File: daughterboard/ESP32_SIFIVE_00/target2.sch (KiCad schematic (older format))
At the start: 0 parts

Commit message: further work on ESP32/SIFIVE daughterboard
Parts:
- added C?: 10u, symbol Device:C_Small
- added R? (x2): 10k, symbol Device:R_Small
- added U?: LoFive-R1, hive_daughterboard:LoFive-R1, symbol hive_daughterboard:LoFive-R1
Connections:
- net +3V3: now also R?.2
- net +5V: now also C?.1, U?.1 (+5V)
- net GPIO2.0: now also U?.24 (GPIO_20/PWM1.0)
- net GPIO2.1: now also U?.25 (GPIO_21/PWM1.2)
- net GPIO2.2: now also U?.26 (GPIO_22/PWM1.3)
- net GPIO2.3: now also U?.27 (GPIO_23)
- net RST_2: now also U?.4 (JTAG_TRST_N)
- net TCK|SWDCLK_2: now also R?.1, U?.5 (JTAG_TCK)
- net TDI|NC_2: now also U?.8 (JTAG_TDI)
- net TDO|SWO_2: now also U?.6 (JTAG_TDO)
- net TMS|SWDIO_2: now also R?.1, U?.7 (JTAG_TMS)
- net UART_RxD2: now also U?.21 (GPIO_17/UART0.TX)
- net UART_TxD2: now also U?.20 (GPIO_16/UART0.RX)
- new net GND: C?.2, R?.2, U?.2 (GND), U?.28 (GND)
- no-connect marks 0 -> 14
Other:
- note removed: "Power"

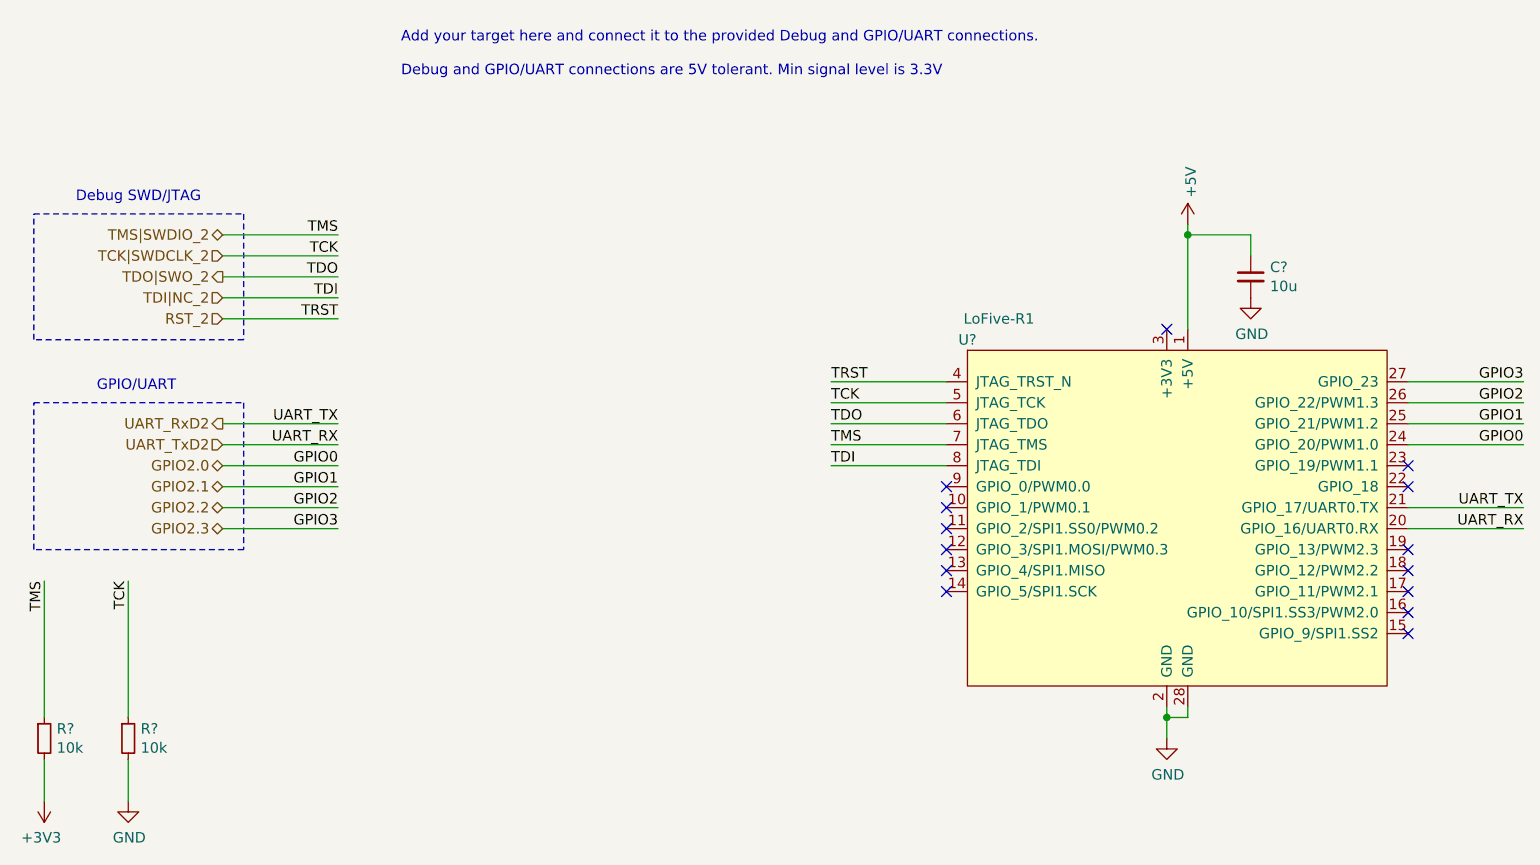
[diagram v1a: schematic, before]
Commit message: ERC on daughterboards
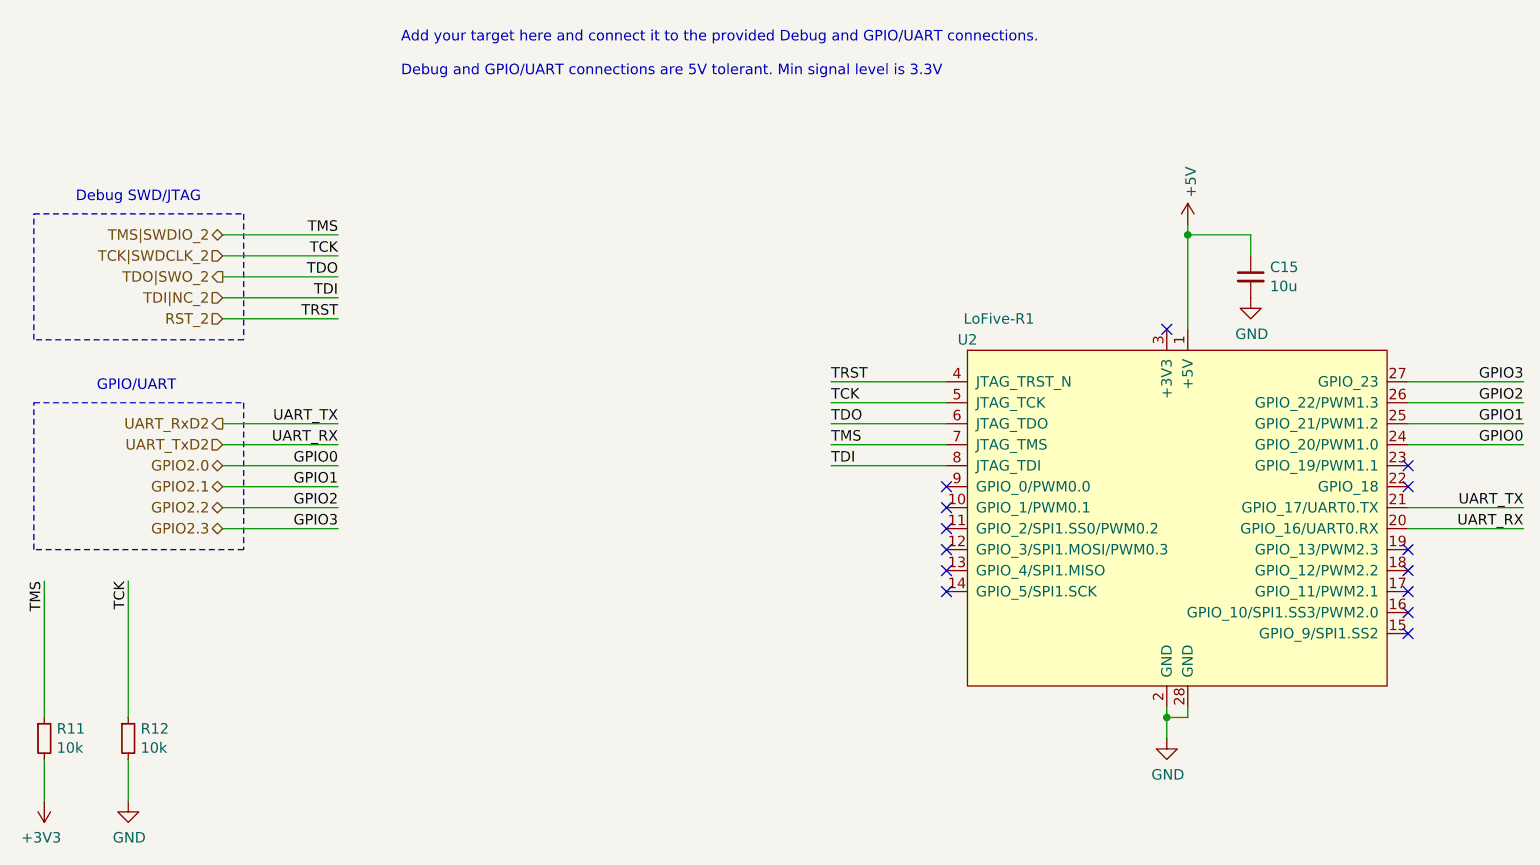
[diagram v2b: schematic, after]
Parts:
- gave numbers to parts that had none: 4
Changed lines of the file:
@@
 Add your target here and connect it to the provided Debug and GPIO/UART connections.\n\nDebug and GPIO/UART connections are 5V tolerant. Min signal level is 3.3V
 $Comp
-L hive_daughterboard:LoFive-R1 U?
+L hive_daughterboard:LoFive-R1 U2
 U 1 1 618DA905
 P 6200 2250
-F 0 "U?" H 5200 2300 50  0000 C CNN
+F 0 "U2" H 5200 2300 50  0000 C CNN
 F 1 "LoFive-R1" H 5350 2400 50  0000 C CNN
 F 2 "hive_daughterboard:LoFive-R1" H 6200 2250 50  0001 C CNN
@@
 P 6250 1650
 AR Path="/61668514/618DDE96" Ref="#PWR?"  Part="1"
-AR Path="/616688D6/618DDE96" Ref="#PWR?"  Part="1"
-F 0 "#PWR?" H 6250 1500 50  0001 C CNN
+AR Path="/616688D6/618DDE96" Ref="#PWR0136"  Part="1"
+F 0 "#PWR0136" H 6250 1500 50  0001 C CNN
 F 1 "+5V" V 6265 1778 50  0000 L CNN
 F 2 "" H 6250 1650 50  0001 C CNN
@@
 $EndComp
 $Comp
-L Device:C_Small C?
+L Device:C_Small C15
 U 1 1 618DFA96
 P 6550 1900
-F 0 "C?" H 6642 1946 50  0000 L CNN
+F 0 "C15" H 6642 1946 50  0000 L CNN
 F 1 "10u" H 6642 1855 50  0000 L CNN
 F 2 "" H 6550 1900 50  0001 C CNN
@@
 NoConn ~ 6150 2150
 $Comp
-L power:GND #PWR?
+L power:GND #PWR0137
 U 1 1 618E074B
 P 6550 2000
-F 0 "#PWR?" H 6550 1750 50  0001 C CNN
+F 0 "#PWR0137" H 6550 1750 50  0001 C CNN
 F 1 "GND" H 6555 1827 50  0000 C CNN
 F 2 "" H 6550 2000 50  0001 C CNN
@@
 	6250 1700 6250 1650
 $Comp
-L power:GND #PWR?
+L power:GND #PWR0138
 U 1 1 618E218D
 P 6150 4100
-F 0 "#PWR?" H 6150 3850 50  0001 C CNN
+F 0 "#PWR0138" H 6150 3850 50  0001 C CNN
 F 1 "GND" H 6155 3927 50  0000 C CNN
 F 2 "" H 6150 4100 50  0001 C CNN
@@
 TMS
 $Comp
-L Device:R_Small R?
+L Device:R_Small R12
 U 1 1 618ED1FE
 P 1200 4100
-F 0 "R?" H 1259 4146 50  0000 L CNN
+F 0 "R12" H 1259 4146 50  0000 L CNN
 F 1 "10k" H 1259 4055 50  0000 L CNN
 F 2 "" H 1200 4100 50  0001 C CNN
@@
 $EndComp
 $Comp
-L power:GND #PWR?
+L power:GND #PWR0139
 U 1 1 618EDFCC
 P 1200 4400
-F 0 "#PWR?" H 1200 4150 50  0001 C CNN
+F 0 "#PWR0139" H 1200 4150 50  0001 C CNN
 F 1 "GND" H 1205 4227 50  0000 C CNN
 F 2 "" H 1200 4400 50  0001 C CNN
@@
 	1200 4400 1200 4200
 $Comp
-L Device:R_Small R?
+L Device:R_Small R11
 U 1 1 618F4230
 P 800 4100
-F 0 "R?" H 859 4146 50  0000 L CNN
+F 0 "R11" H 859 4146 50  0000 L CNN
 F 1 "10k" H 859 4055 50  0000 L CNN
 F 2 "" H 800 4100 50  0001 C CNN
@@
 	800  3350 800  4000
 $Comp
-L power:+3V3 #PWR?
+L power:+3V3 #PWR0140
 U 1 1 618F94CF
 P 800 4400
-F 0 "#PWR?" H 800 4250 50  0001 C CNN
+F 0 "#PWR0140" H 800 4250 50  0001 C CNN
 F 1 "+3V3" H 815 4573 50  0000 C CNN
 F 2 "" H 800 4400 50  0001 C CNN

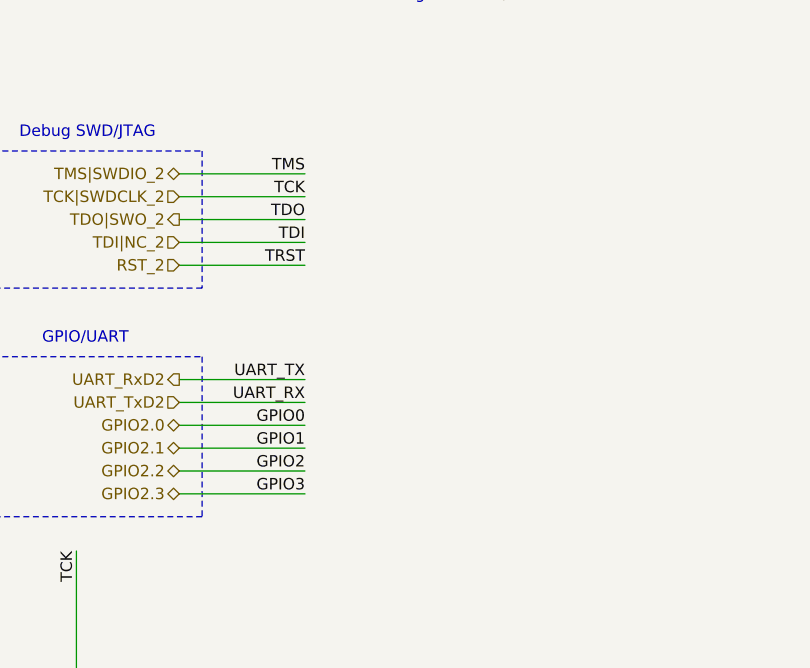
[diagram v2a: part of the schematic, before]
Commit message: added testpoints to daughterboards, updated readme
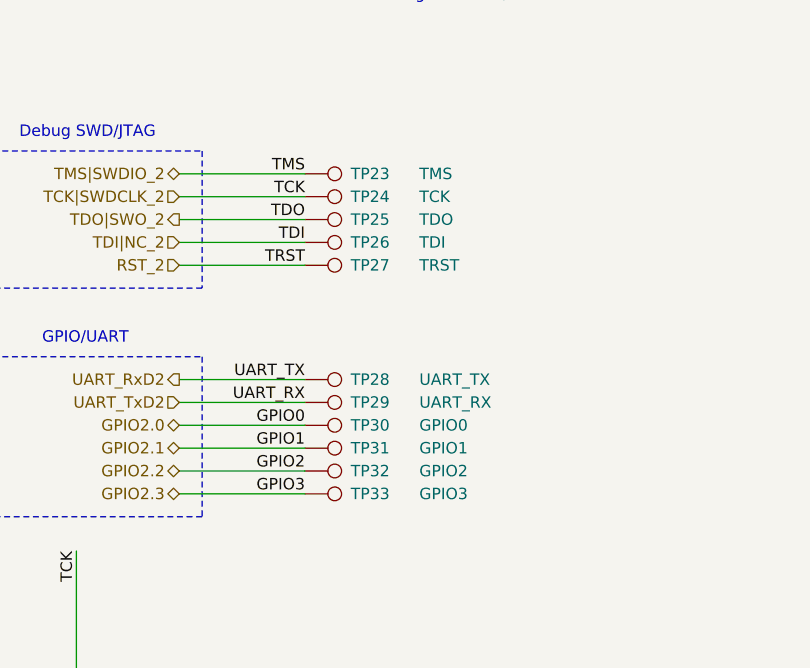
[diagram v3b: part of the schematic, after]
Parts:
- added TP23: TMS, symbol Connector:TestPoint
- added TP24: TCK, symbol Connector:TestPoint
- added TP25: TDO, symbol Connector:TestPoint
- added TP26: TDI, symbol Connector:TestPoint
- added TP27: TRST, symbol Connector:TestPoint
- added TP28: UART_TX, symbol Connector:TestPoint
- added TP29: UART_RX, symbol Connector:TestPoint
- added TP30: GPIO0, symbol Connector:TestPoint
- added TP31: GPIO1, symbol Connector:TestPoint
- added TP32: GPIO2, symbol Connector:TestPoint
- added TP33: GPIO3, symbol Connector:TestPoint
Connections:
- net GPIO2.0: now also TP30.1
- net GPIO2.1: now also TP31.1
- net GPIO2.2: now also TP32.1
- net GPIO2.3: now also TP33.1
- net RST_2: now also TP27.1
- net TCK|SWDCLK_2: now also TP24.1
- net TDI|NC_2: now also TP26.1
- net TDO|SWO_2: now also TP25.1
- net TMS|SWDIO_2: now also TP23.1
- net UART_RxD2: now also TP28.1
- net UART_TxD2: now also TP29.1
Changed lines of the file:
@@
 	-1   0    0    1
 $EndComp
+$Comp
+L Connector:TestPoint TP23
+U 1 1 61906846
+P 2200 1700
+F 0 "TP23" V 2200 1900 50  0000 L CNN
+F 1 "TMS" V 2200 2200 50  0000 L CNN
+F 2 "" H 2400 1700 50  0001 C CNN
+F 3 "~" H 2400 1700 50  0001 C CNN
+	1    2200 1700
+	0    1    1    0
+$EndComp
+$Comp
+L Connector:TestPoint TP24
+U 1 1 6190873D
+P 2200 1800
+F 0 "TP24" V 2200 2000 50  0000 L CNN
+F 1 "TCK" V 2200 2300 50  0000 L CNN
+F 2 "" H 2400 1800 50  0001 C CNN
+F 3 "~" H 2400 1800 50  0001 C CNN
+	1    2200 1800
+	0    1    1    0
+$EndComp
+$Comp
+L Connector:TestPoint TP25
+U 1 1 619088C7
+P 2200 1900
+F 0 "TP25" V 2200 2100 50  0000 L CNN
+F 1 "TDO" V 2200 2400 50  0000 L CNN
+F 2 "" H 2400 1900 50  0001 C CNN
+F 3 "~" H 2400 1900 50  0001 C CNN
+	1    2200 1900
+	0    1    1    0
+$EndComp
+$Comp
+L Connector:TestPoint TP26
+U 1 1 61908AEF
+P 2200 2000
+F 0 "TP26" V 2200 2200 50  0000 L CNN
+F 1 "TDI" V 2200 2500 50  0000 L CNN
+F 2 "" H 2400 2000 50  0001 C CNN
+F 3 "~" H 2400 2000 50  0001 C CNN
+	1    2200 2000
+	0    1    1    0
+$EndComp
+$Comp
+L Connector:TestPoint TP27
+U 1 1 61908CE1
+P 2200 2100
+F 0 "TP27" V 2200 2300 50  0000 L CNN
+F 1 "TRST" V 2200 2600 50  0000 L CNN
+F 2 "" H 2400 2100 50  0001 C CNN
+F 3 "~" H 2400 2100 50  0001 C CNN
+	1    2200 2100
+	0    1    1    0
+$EndComp
+$Comp
+L Connector:TestPoint TP28
+U 1 1 61908F07
+P 2200 2600
+F 0 "TP28" V 2200 2800 50  0000 L CNN
+F 1 "UART_TX" V 2200 3100 50  0000 L CNN
+F 2 "" H 2400 2600 50  0001 C CNN
+F 3 "~" H 2400 2600 50  0001 C CNN
+	1    2200 2600
+	0    1    1    0
+$EndComp
+$Comp
+L Connector:TestPoint TP29
+U 1 1 61909318
+P 2200 2700
+F 0 "TP29" V 2200 2900 50  0000 L CNN
+F 1 "UART_RX" V 2200 3200 50  0000 L CNN
+F 2 "" H 2400 2700 50  0001 C CNN
+F 3 "~" H 2400 2700 50  0001 C CNN
+	1    2200 2700
+	0    1    1    0
+$EndComp
+$Comp
+L Connector:TestPoint TP30
+U 1 1 6190965A
+P 2200 2800
+F 0 "TP30" V 2200 3000 50  0000 L CNN
+F 1 "GPIO0" V 2200 3300 50  0000 L CNN
+F 2 "" H 2400 2800 50  0001 C CNN
+F 3 "~" H 2400 2800 50  0001 C CNN
+	1    2200 2800
+	0    1    1    0
+$EndComp
+$Comp
+L Connector:TestPoint TP31
+U 1 1 619098B5
+P 2200 2900
+F 0 "TP31" V 2200 3100 50  0000 L CNN
+F 1 "GPIO1" V 2200 3400 50  0000 L CNN
+F 2 "" H 2400 2900 50  0001 C CNN
+F 3 "~" H 2400 2900 50  0001 C CNN
+	1    2200 2900
+	0    1    1    0
+$EndComp
+$Comp
+L Connector:TestPoint TP32
+U 1 1 61909B12
+P 2200 3000
+F 0 "TP32" V 2200 3200 50  0000 L CNN
+F 1 "GPIO2" V 2200 3500 50  0000 L CNN
+F 2 "" H 2400 3000 50  0001 C CNN
+F 3 "~" H 2400 3000 50  0001 C CNN
+	1    2200 3000
+	0    1    1    0
+$EndComp
+$Comp
+L Connector:TestPoint TP33
+U 1 1 61909D32
+P 2200 3100
+F 0 "TP33" V 2200 3300 50  0000 L CNN
+F 1 "GPIO3" V 2200 3600 50  0000 L CNN
+F 2 "" H 2400 3100 50  0001 C CNN
+F 3 "~" H 2400 3100 50  0001 C CNN
+	1    2200 3100
+	0    1    1    0
+$EndComp
 $EndSCHEMATC

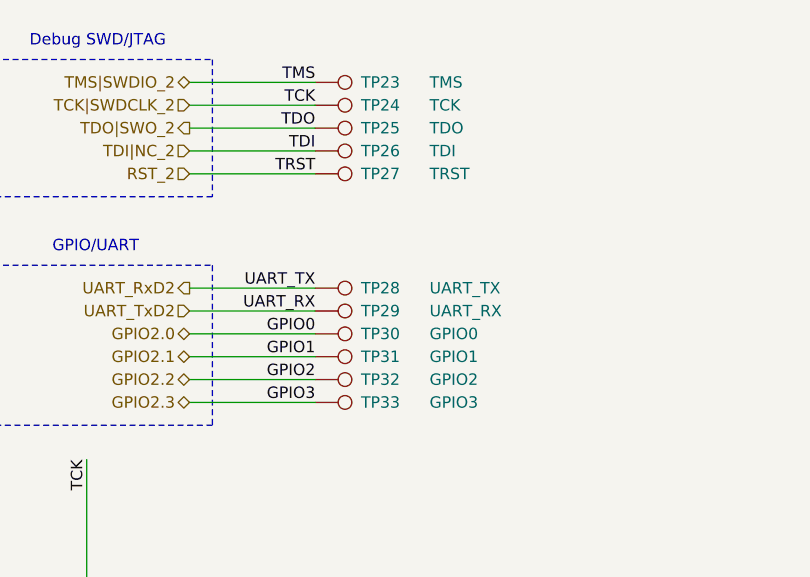
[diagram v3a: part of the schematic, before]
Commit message: started with esp32/sifive layout
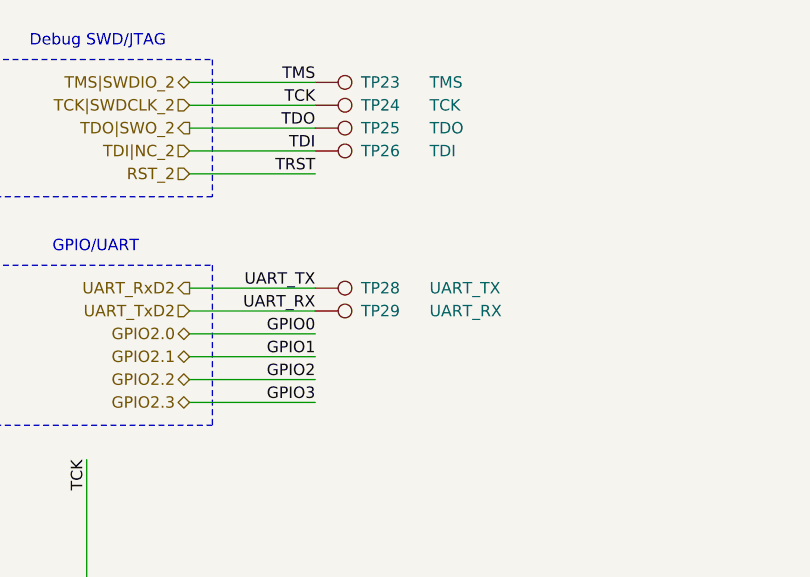
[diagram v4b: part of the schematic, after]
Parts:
- removed TP27: TRST, symbol Connector:TestPoint
- removed TP30: GPIO0, symbol Connector:TestPoint
- removed TP31: GPIO1, symbol Connector:TestPoint
- removed TP32: GPIO2, symbol Connector:TestPoint
- removed TP33: GPIO3, symbol Connector:TestPoint
- C15: footprint (none) -> Capacitor_SMD:C_0603_1608Metric_Pad1.05x0.95mm_HandSolder
- R11, R12: footprint (none) -> Resistor_SMD:R_0603_1608Metric_Pad1.05x0.95mm_HandSolder
- TP23, TP24, TP25, TP26, TP28, TP29: footprint (none) -> TestPoint:TestPoint_Pad_1.0x1.0mm
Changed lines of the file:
@@
 F 0 "C15" H 6642 1946 50  0000 L CNN
 F 1 "10u" H 6642 1855 50  0000 L CNN
-F 2 "" H 6550 1900 50  0001 C CNN
+F 2 "Capacitor_SMD:C_0603_1608Metric_Pad1.05x0.95mm_HandSolder" H 6550 1900 50  0001 C CNN
 F 3 "~" H 6550 1900 50  0001 C CNN
 	1    6550 1900
@@
 F 0 "R12" H 1259 4146 50  0000 L CNN
 F 1 "10k" H 1259 4055 50  0000 L CNN
-F 2 "" H 1200 4100 50  0001 C CNN
+F 2 "Resistor_SMD:R_0603_1608Metric_Pad1.05x0.95mm_HandSolder" H 1200 4100 50  0001 C CNN
 F 3 "~" H 1200 4100 50  0001 C CNN
 	1    1200 4100
@@
 F 0 "R11" H 859 4146 50  0000 L CNN
 F 1 "10k" H 859 4055 50  0000 L CNN
-F 2 "" H 800 4100 50  0001 C CNN
+F 2 "Resistor_SMD:R_0603_1608Metric_Pad1.05x0.95mm_HandSolder" H 800 4100 50  0001 C CNN
 F 3 "~" H 800 4100 50  0001 C CNN
 	1    800  4100
@@
 F 0 "TP23" V 2200 1900 50  0000 L CNN
 F 1 "TMS" V 2200 2200 50  0000 L CNN
-F 2 "" H 2400 1700 50  0001 C CNN
+F 2 "TestPoint:TestPoint_Pad_1.0x1.0mm" H 2400 1700 50  0001 C CNN
 F 3 "~" H 2400 1700 50  0001 C CNN
 	1    2200 1700
@@
 F 0 "TP24" V 2200 2000 50  0000 L CNN
 F 1 "TCK" V 2200 2300 50  0000 L CNN
-F 2 "" H 2400 1800 50  0001 C CNN
+F 2 "TestPoint:TestPoint_Pad_1.0x1.0mm" H 2400 1800 50  0001 C CNN
 F 3 "~" H 2400 1800 50  0001 C CNN
 	1    2200 1800
@@
 F 0 "TP25" V 2200 2100 50  0000 L CNN
 F 1 "TDO" V 2200 2400 50  0000 L CNN
-F 2 "" H 2400 1900 50  0001 C CNN
+F 2 "TestPoint:TestPoint_Pad_1.0x1.0mm" H 2400 1900 50  0001 C CNN
 F 3 "~" H 2400 1900 50  0001 C CNN
 	1    2200 1900
@@
 F 0 "TP26" V 2200 2200 50  0000 L CNN
 F 1 "TDI" V 2200 2500 50  0000 L CNN
-F 2 "" H 2400 2000 50  0001 C CNN
+F 2 "TestPoint:TestPoint_Pad_1.0x1.0mm" H 2400 2000 50  0001 C CNN
 F 3 "~" H 2400 2000 50  0001 C CNN
 	1    2200 2000
-	0    1    1    0
-$EndComp
-$Comp
-L Connector:TestPoint TP27
-U 1 1 61908CE1
-P 2200 2100
-F 0 "TP27" V 2200 2300 50  0000 L CNN
-F 1 "TRST" V 2200 2600 50  0000 L CNN
-F 2 "" H 2400 2100 50  0001 C CNN
-F 3 "~" H 2400 2100 50  0001 C CNN
-	1    2200 2100
 	0    1    1    0
 $EndComp
@@
 F 0 "TP28" V 2200 2800 50  0000 L CNN
 F 1 "UART_TX" V 2200 3100 50  0000 L CNN
-F 2 "" H 2400 2600 50  0001 C CNN
+F 2 "TestPoint:TestPoint_Pad_1.0x1.0mm" H 2400 2600 50  0001 C CNN
 F 3 "~" H 2400 2600 50  0001 C CNN
 	1    2200 2600
@@
 F 0 "TP29" V 2200 2900 50  0000 L CNN
 F 1 "UART_RX" V 2200 3200 50  0000 L CNN
-F 2 "" H 2400 2700 50  0001 C CNN
+F 2 "TestPoint:TestPoint_Pad_1.0x1.0mm" H 2400 2700 50  0001 C CNN
 F 3 "~" H 2400 2700 50  0001 C CNN
 	1    2200 2700
 	0    1    1    0
 $EndComp
-$Comp
-L Connector:TestPoint TP30
-U 1 1 6190965A
-P 2200 2800
-F 0 "TP30" V 2200 3000 50  0000 L CNN
-F 1 "GPIO0" V 2200 3300 50  0000 L CNN
-F 2 "" H 2400 2800 50  0001 C CNN
-F 3 "~" H 2400 2800 50  0001 C CNN
-	1    2200 2800
-	0    1    1    0
-$EndComp
-$Comp
-L Connector:TestPoint TP31
-U 1 1 619098B5
-P 2200 2900
-F 0 "TP31" V 2200 3100 50  0000 L CNN
-F 1 "GPIO1" V 2200 3400 50  0000 L CNN
-F 2 "" H 2400 2900 50  0001 C CNN
-F 3 "~" H 2400 2900 50  0001 C CNN
-	1    2200 2900
-	0    1    1    0
-$EndComp
-$Comp
-L Connector:TestPoint TP32
-U 1 1 61909B12
-P 2200 3000
-F 0 "TP32" V 2200 3200 50  0000 L CNN
-F 1 "GPIO2" V 2200 3500 50  0000 L CNN
-F 2 "" H 2400 3000 50  0001 C CNN
-F 3 "~" H 2400 3000 50  0001 C CNN
-	1    2200 3000
-	0    1    1    0
-$EndComp
-$Comp
-L Connector:TestPoint TP33
-U 1 1 61909D32
-P 2200 3100
-F 0 "TP33" V 2200 3300 50  0000 L CNN
-F 1 "GPIO3" V 2200 3600 50  0000 L CNN
-F 2 "" H 2400 3100 50  0001 C CNN
-F 3 "~" H 2400 3100 50  0001 C CNN
-	1    2200 3100
-	0    1    1    0
-$EndComp
